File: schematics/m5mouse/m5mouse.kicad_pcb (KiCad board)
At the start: 2 copper layers, 117.5 x 50 mm, 93 parts, among them IC1 LM3940IMP-3.3_NOPB, J1 Conn_01x02, J2 M-BUS, J3 SWD, J4 Conn_02x03_Odd_Even, J5 Conn_02x03_Odd_Even, J6 Conn_01x03, J7 Conn_01x06, J8 Conn_01x06, Q1 BSS138, Q2 ST-1KL3A, Q3 BSS138, Q4 ST-1KL3A, Q5 BSS138, Q6 ST-1KL3A, Q7 BSS138, Q8 ST-1KL3A, SW1 SW_SPDT, SW2 SW_Push, U1 TPS562200, U2 STM32F405RGTx, U3 DRV8835, U4 MPU9250_9255, Y1 8MHz, Y2 32.768kHz

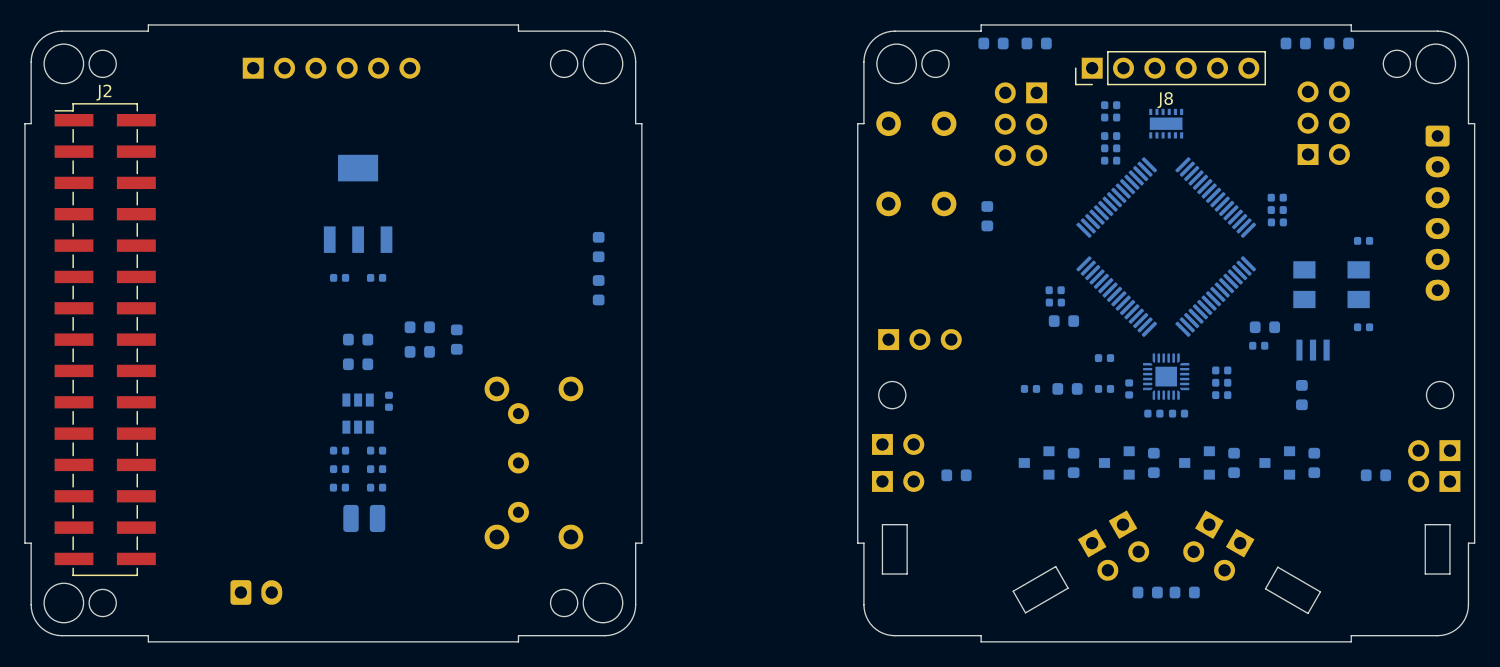
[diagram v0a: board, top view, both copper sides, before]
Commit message: Adjust parts positions
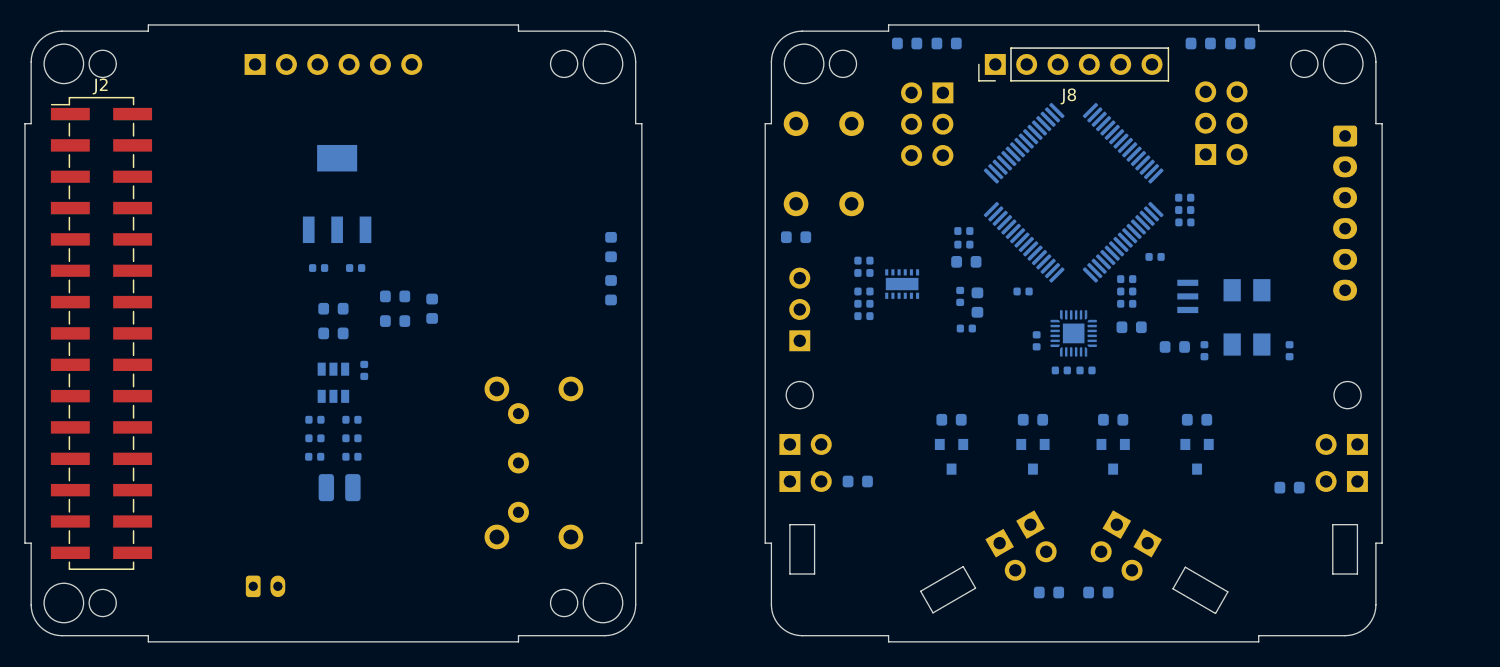
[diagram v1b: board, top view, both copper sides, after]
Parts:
- D2, D3, D4, D5, Q2, Q4, Q6, Q8: footprint Connector_PinHeader_2.54mm:PinHeader_1x02_P2.54mm_Vertical -> m5mouse:ThroughHole_1x02_P2.54_Vertical
- J1: footprint Connector_JST:JST_EH_B2B-EH-A_1x02_P2.50mm_Vertical -> Connector_JST:JST_PH_B2B-PH-K_1x02_P2.00mm_Vertical
- moved U3 25.0 mm to (151.1, 111.0)
- moved C13 23.6 mm to (148.0, 112.6)
- moved C20 23.6 mm to (148.0, 110.1)
- moved C21 23.6 mm to (148.0, 111.6)
- moved C24 23.6 mm to (148.0, 113.6)
- moved C25 23.6 mm to (148.0, 109.1)
- moved R14 15.6 mm to (142.5, 107.2), turned to 0 degrees
- moved FB1 14.9 mm to (169.7, 114.5), turned to 180 degrees
- moved C18 13.9 mm to (155.8, 112.0), turned to 270 degrees
- moved C9 13.0 mm to (175.6, 116.4), turned to 90 degrees
- moved Y1 12.9 mm to (174.9, 110.4), turned to 270 degrees
- moved C22 11.1 mm to (171.6, 108.8)
- moved C8 10.7 mm to (182.5, 116.4), turned to 270 degrees
- moved C15 10.7 mm to (169.3, 110.6)
- moved C16 10.7 mm to (169.3, 111.6)
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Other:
- board size 117.5 x 50 mm -> 110 x 50 mm

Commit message: Draw pattern
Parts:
- added MH10: MountingHole_2.2mm_M2, MountingHole:MountingHole_2.2mm_M2, F.Cu at (165.0, 137.0)
- added MH9: MountingHole_2.2mm_M2, MountingHole:MountingHole_2.2mm_M2, F.Cu at (105.0, 137.0)
- moved C13 21.3 mm to (160.8, 95.6)
- moved C24 21.3 mm to (160.8, 96.6)
- moved C22 9.54 mm to (176.8, 116.8), turned to 270 degrees
- moved C14 7.47 mm to (173.0, 98.6), turned to 270 degrees
- moved C10 6.71 mm to (172.0, 98.6), turned to 90 degrees
- moved C9 3.82 mm to (179.4, 116.8), turned to 270 degrees
- moved C5 3.61 mm to (108.5, 125.0), turned to 270 degrees
- moved R4 3.35 mm to (173.8, 112.8), turned to 270 degrees
- moved C28 2.80 mm to (174.0, 106.8)
- moved R11 2.61 mm to (160.8, 137.4), turned to 270 degrees
- moved R9 2.61 mm to (169.2, 137.4), turned to 270 degrees
- moved FB1 2.55 mm to (171.6, 112.8), turned to 270 degrees
- moved Y1 2.48 mm to (176.8, 108.8)
- moved C8 2.14 mm to (180.4, 116.8)
- moved Y2 2.05 mm to (180.2, 112.0)
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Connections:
- U2 pad 52: GPIO11 -> Net-(U2-Pad52)
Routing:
- net +3V3: track 0.00 -> 157.1 mm, vias 0 -> 7
- net GND: track 0.00 -> 149.9 mm, vias 0 -> 90
- net VIN: track 0.00 -> 103.0 mm, vias 0 -> 1
- net +3.3VA: track 0.00 -> 100.3 mm, vias 0 -> 2
- net +5V: track 0.00 -> 93.0 mm, vias 0 -> 5
- net Net-(C19-Pad1): track 0.00 -> 73.3 mm, vias 0 -> 1
- net ADC_BAT: track 0.00 -> 40.8 mm, vias 0 -> 1
- net M5_I2C1_SDA: track 0.00 -> 38.0 mm
- net SWO: track 0.00 -> 38.0 mm, vias 0 -> 1
- net M5_I2C1_SCL: track 0.00 -> 37.7 mm
- net ADC1_IN2: track 0.00 -> 37.4 mm, vias 0 -> 1
- net BOOT: track 0.00 -> 36.1 mm, vias 0 -> 2
- net ADC1_IN0: track 0.00 -> 34.1 mm, vias 0 -> 1
- net /Motor_Module/BOUT2: track 0.00 -> 33.0 mm
- net /Motor_Module/BOUT1: track 0.00 -> 31.6 mm
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- added copper zone on B.Cu, net +5V
- added copper zone on F.Cu, net +5V
- added copper zone on B.Cu, net GND
- added copper zone on F.Cu, net GND
- added copper zone on B.Cu, net VIN

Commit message: Fix path
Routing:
- net +5V: track 93.0 -> 112.7 mm, vias 5 -> 6
- net BOOT: track 36.1 -> 42.6 mm
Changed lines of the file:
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@@
     (thickness 1.6)
     (drawings 84)
-    (tracks 832)
+    (tracks 841)
     (zones 0)
     (modules 95)
@@
   )
   (setup
-    (last_trace_width 0.4)
+    (last_trace_width 0.2)
     (user_trace_width 0.2)
     (user_trace_width 0.4)
@@
     (aux_axis_origin 80 140)
     (grid_origin 80 140)
-    (visible_elements FFFFF7FF)
+    (visible_elements FFFFFFFF)
     (pcbplotparams
       (layerselection 0x010fc_ffffffff)
@@
   (segment (start 108.8 106.6) (end 111 104.4) (width 0.6) (layer B.Cu) (net 5))
   (segment (start 111 95.39) (end 108.81 93.2) (width 0.6) (layer F.Cu) (net 5))
-  (segment (start 111 104.4) (end 111 95.39) (width 0.6) (layer F.Cu) (net 5))
   (segment (start 107.285 111.5025) (end 108.5875 110.2) (width 0.6) (layer B.Cu) (net 5))
   (via (at 110.8 110.2) (size 0.6) (drill 0.3) (layers F.Cu B.Cu) (net 5))
   (segment (start 108.5875 110.2) (end 110.8 110.2) (width 0.6) (layer B.Cu) (net 5))
+  (segment (start 111 104.4) (end 111 102.2) (width 0.6) (layer F.Cu) (net 5))
+  (segment (start 111 102.2) (end 111 95.39) (width 0.6) (layer F.Cu) (net 5))
+  (via (at 126.2 104) (size 0.6) (drill 0.3) (layers F.Cu B.Cu) (net 5))
+  (segment (start 127.5 105.3) (end 126.2 104) (width 0.4) (layer B.Cu) (net 5))
+  (segment (start 127.5 107.2125) (end 127.5 105.3) (width 0.4) (layer B.Cu) (net 5))
+  (segment (start 125.775736 104) (end 126.2 104) (width 0.4) (layer F.Cu) (net 5))
+  (segment (start 114.8 104) (end 125.775736 104) (width 0.4) (layer F.Cu) (net 5))
+  (segment (start 111 102.2) (end 113 102.2) (width 0.4) (layer F.Cu) (net 5))
+  (segment (start 113 102.2) (end 114.8 104) (width 0.4) (layer F.Cu) (net 5))
   (segment (start 173.489088 108.2) (end 170.957375 105.668287) (width 0.2) (layer B.Cu) (net 6))
   (segment (start 182.8 115.4) (end 182.8 111.2) (width 0.2) (layer B.Cu) (net 6))
@@
   (segment (start 162.6 96.6) (end 161.285 96.6) (width 0.2) (layer B.Cu) (net 13))
   (segment (start 162.763401 96.763401) (end 162.6 96.6) (width 0.2) (layer B.Cu) (net 13))
-  (segment (start 127.5 108.7875) (end 127.5 110.7125) (width 0.2) (layer B.Cu) (net 14))
+  (segment (start 127.5 108.7875) (end 127.5 110.7125) (width 0.4) (layer B.Cu) (net 14))
   (segment (start 175 126) (end 175.6 126) (width 0.2) (layer B.Cu) (net 15))
   (via (at 177.6 124) (size 0.6) (drill 0.3) (layers F.Cu B.Cu) (net 15))
@@
   (segment (start 145.997599 94.502401) (end 142.5 98) (width 0.2) (layer B.Cu) (net 77))
   (segment (start 155 93.8) (end 147.651554 93.8) (width 0.2) (layer B.Cu) (net 77))
+  (segment (start 142.5 104.5) (end 142.5 98) (width 0.2) (layer B.Cu) (net 77))
   (segment (start 157.525126 108.6) (end 156.9875 108.6) (width 0.2) (layer B.Cu) (net 78))
   (segment (start 159.749732 106.375394) (end 157.525126 108.6) (width 0.2) (layer B.Cu) (net 78))
@@
     (connect_pads (clearance 0.508))
     (min_thickness 0.254)
-    (fill (arc_segments 32) (thermal_gap 0.508) (thermal_bridge_width 0.508))
+    (fill yes (arc_segments 32) (thermal_gap 0.508) (thermal_bridge_width 0.508))
     (polygon
       (pts
@@
     (connect_pads (clearance 0.508))
     (min_thickness 0.254)
-    (fill (arc_segments 32) (thermal_gap 0.508) (thermal_bridge_width 0.508))
+    (fill yes (arc_segments 32) (thermal_gap 0.508) (thermal_bridge_width 0.508))
     (polygon
       (pts
@@
     (connect_pads (clearance 0.508))
     (min_thickness 0.254)
-    (fill (arc_segments 32) (thermal_gap 0.508) (thermal_bridge_width 0.508))
+    (fill yes (arc_segments 32) (thermal_gap 0.508) (thermal_bridge_width 0.508))
     (polygon
       (pts
@@
     (connect_pads (clearance 0.508))
     (min_thickness 0.254)
-    (fill (arc_segments 32) (thermal_gap 0.508) (thermal_bridge_width 0.508))
+    (fill yes (arc_segments 32) (thermal_gap 0.508) (thermal_bridge_width 0.508))
     (polygon
       (pts
@@
     (connect_pads (clearance 0.508))
     (min_thickness 0.254)
-    (fill (arc_segments 32) (thermal_gap 0.508) (thermal_bridge_width 0.508))
+    (fill yes (arc_segments 32) (thermal_gap 0.508) (thermal_bridge_width 0.508))
     (polygon
       (pts
@@
     (connect_pads (clearance 0.508))
     (min_thickness 0.254)
-    (fill (arc_segments 32) (thermal_gap 0.508) (thermal_bridge_width 0.508))
+    (fill yes (arc_segments 32) (thermal_gap 0.508) (thermal_bridge_width 0.508))
     (polygon
       (pts
@@
     (connect_pads (clearance 0.508))
     (min_thickness 0.254)
-    (fill (arc_segments 32) (thermal_gap 0.508) (thermal_bridge_width 0.508))
+    (fill yes (arc_segments 32) (thermal_gap 0.508) (thermal_bridge_width 0.508))
     (polygon
       (pts
@@
     (connect_pads (clearance 0.508))
     (min_thickness 0.254)
-    (fill (arc_segments 32) (thermal_gap 0.508) (thermal_bridge_width 0.508))
+    (fill yes (arc_segments 32) (thermal_gap 0.508) (thermal_bridge_width 0.508))
     (polygon
       (pts

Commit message: Fix path
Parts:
- added G***: LOGO, mod:RT_mark1_30x30, F.Cu at (104.8, 111.6)
- added G***: LOGO, mod:RT_mark1_30x30, F.Cu at (163.6, 111.4)
- moved R4 2.44 mm to (175.8, 114.2), turned to 90 degrees
- moved C14 0.85 mm to (172.4, 98.0), turned to 0 degrees
- moved C10 0.57 mm to (172.4, 99.0), turned to 180 degrees
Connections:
- C15 pad 1: GND -> GNDA
- C16 pad 1: GND -> GNDA
- C17 pad 1: GND -> GNDA
- Q1 pad 1: GPIO2 -> GPIO4
- Q3 pad 1: GPIO3 -> GPIO5
- Q5 pad 1: GPIO4 -> GPIO2
- Q7 pad 1: GPIO5 -> GPIO3
- R10 pad 1: GPIO4 -> GPIO2
- R11 pad 2: GND -> GNDA
- R12 pad 1: GPIO5 -> GPIO3
- R13 pad 2: GND -> GNDA
- R6 pad 1: GPIO2 -> GPIO4
- R7 pad 2: GND -> GNDA
- R8 pad 1: GPIO3 -> GPIO5
- R9 pad 2: GND -> GNDA
- U2 pad 12: GND -> GNDA
- U2 pad 34: GPIO10 -> Net-(U2-Pad34)
- U2 pad 50: Net-(U2-Pad50) -> GPIO10
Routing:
- net GND: track 149.9 -> 64.5 mm, vias 90 -> 79
- net GNDA: track 0.00 -> 81.4 mm, vias 0 -> 10
- net +3V3: track 157.1 -> 200.0 mm
- net GPIO10: track 26.0 -> 15.0 mm, vias 4 -> 2
- net GPIO4: track 17.2 -> 28.2 mm
- net GPIO2: track 29.9 -> 19.0 mm
- net Net-(R4-Pad1): track 6.90 -> 10.7 mm
- net BOOT: track 42.6 -> 46.2 mm
- net /Motor_Module/AOUT1: track 19.6 -> 22.7 mm
- net SWO: track 38.0 -> 34.9 mm
- net SWCLK: track 28.7 -> 25.8 mm
- net GPIO3: track 22.4 -> 19.7 mm
- net TIM3_CH1: track 12.9 -> 15.0 mm
- net GPIO5: track 20.2 -> 22.1 mm
- net +3.3VA: track 100.3 -> 98.4 mm
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- added copper zone on B.Cu, net GNDA
- added copper zone on F.Cu, net GNDA
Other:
- board text added: "M5Mouse/MouseUnit v0.1 @meganetaaan"
- board text added: "M5Mouse/PowerUnit v0.1 @meganetaaan"

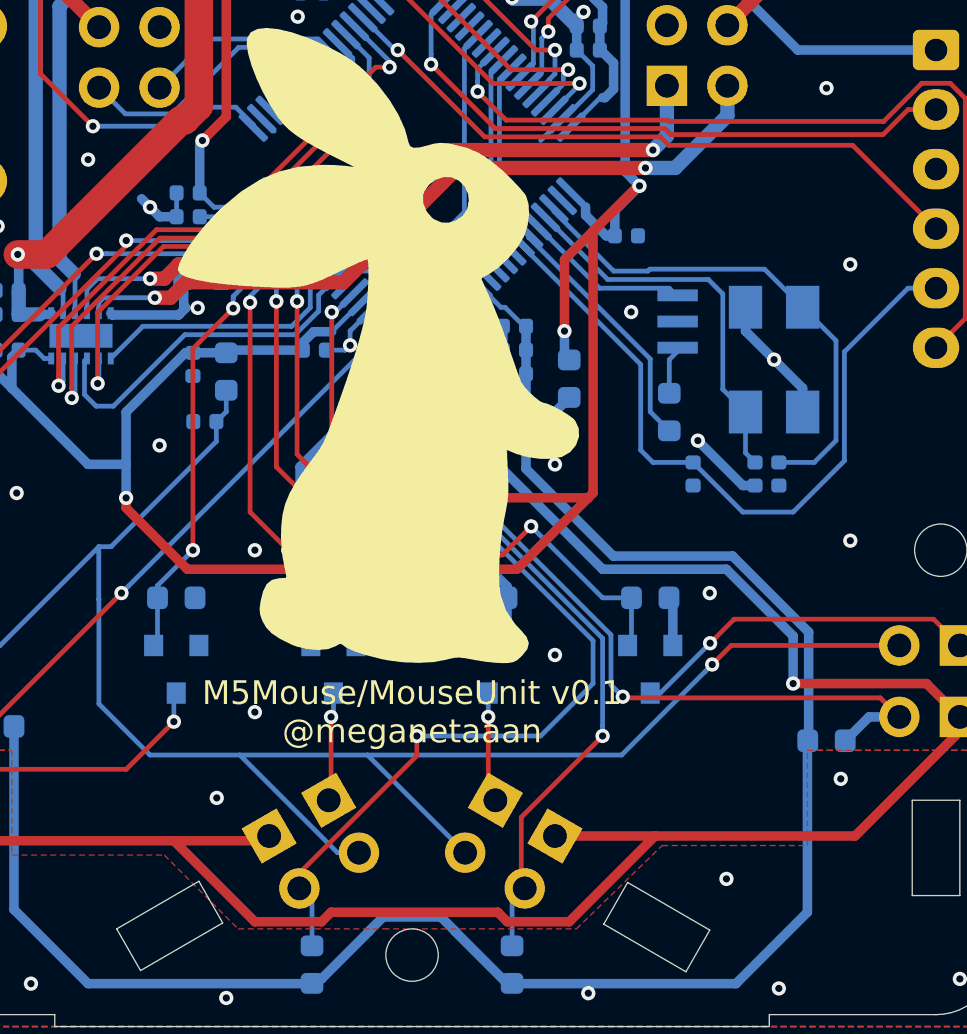
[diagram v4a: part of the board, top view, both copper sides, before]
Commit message: Connect GNDA and GND via ferrite bead
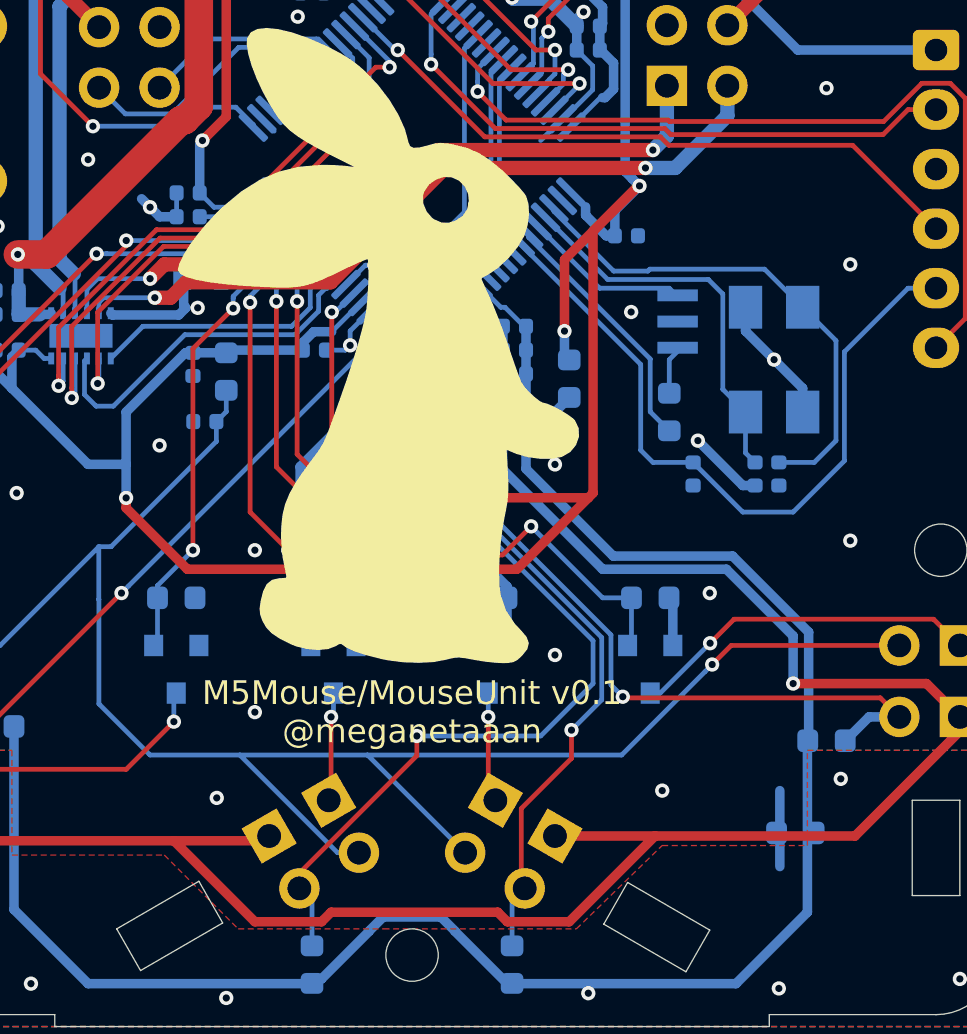
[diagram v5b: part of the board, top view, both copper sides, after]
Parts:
- added FB2: Ferrite_Bead_Small, Resistor_SMD:R_0603_1608Metric, B.Cu at (181.1, 131.9)
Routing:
- net GND: track 64.5 -> 67.7 mm, vias 79 -> 80
- net GNDA: vias 10 -> 9

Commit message: Fix path
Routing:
- net GND: track 67.7 -> 73.7 mm, vias 80 -> 82
- net SWCLK: track 25.8 -> 27.3 mm
- net GPIO7: track 22.6 -> 21.3 mm
- net GPIO6: track 23.3 -> 22.3 mm
- net SWDIO: track 27.7 -> 28.6 mm
- net GPIO8: track 24.5 -> 23.8 mm
